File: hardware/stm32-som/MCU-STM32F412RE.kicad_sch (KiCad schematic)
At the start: 33 parts

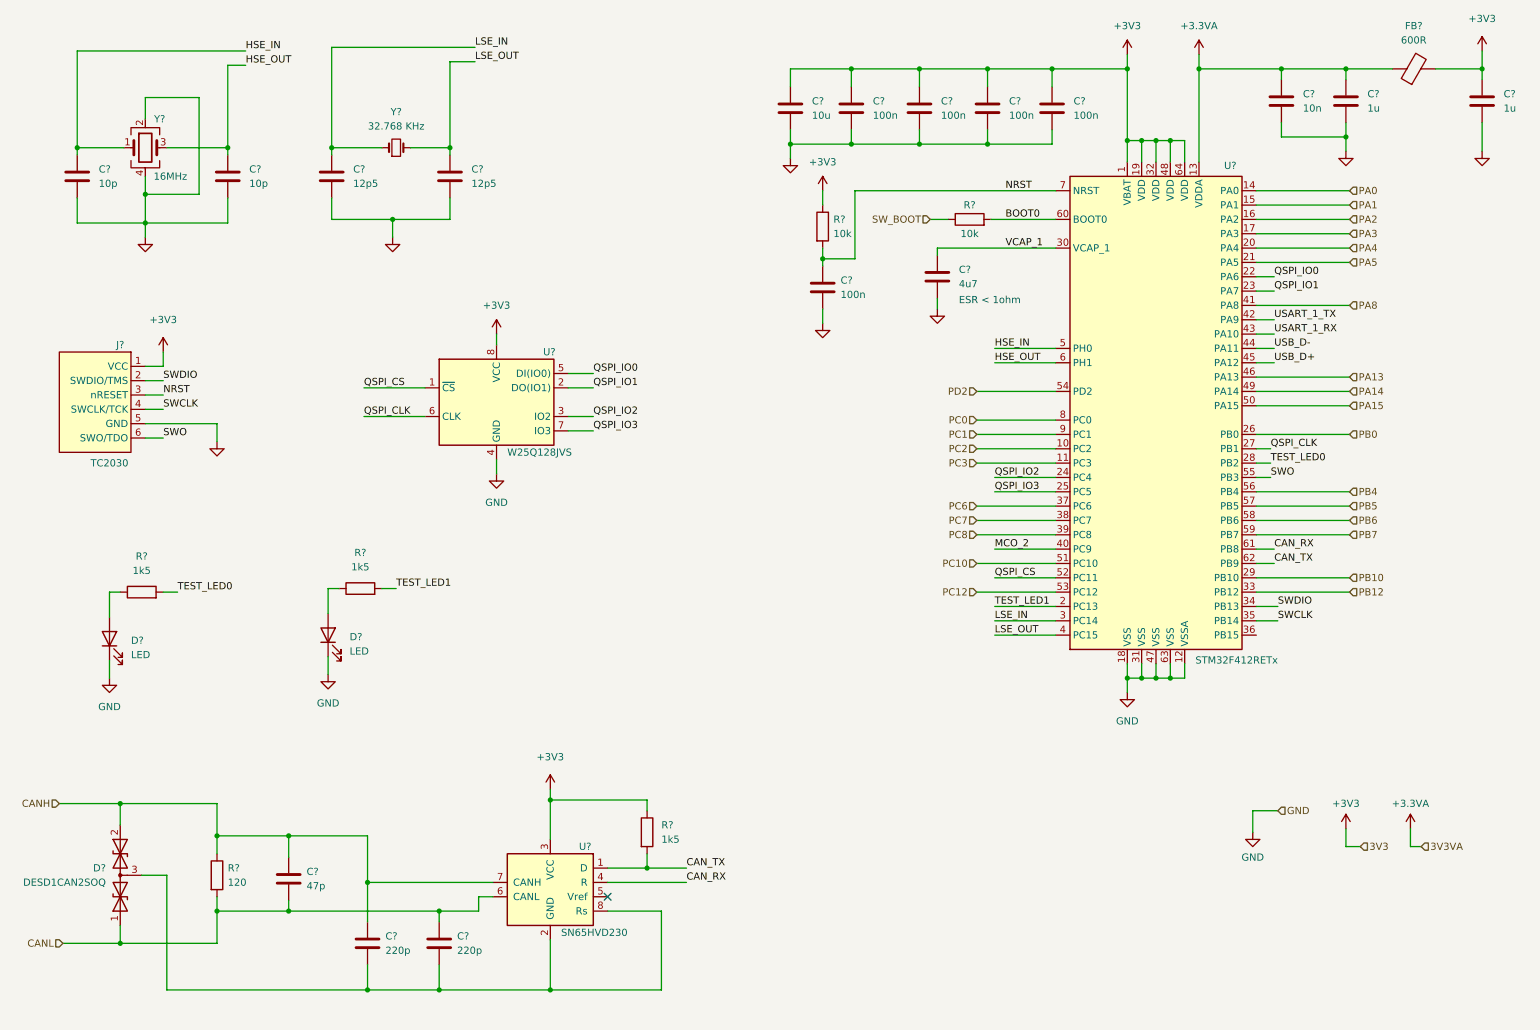
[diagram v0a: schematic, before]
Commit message: add test points, complete top hierarchical level, correct jtag mcu connection
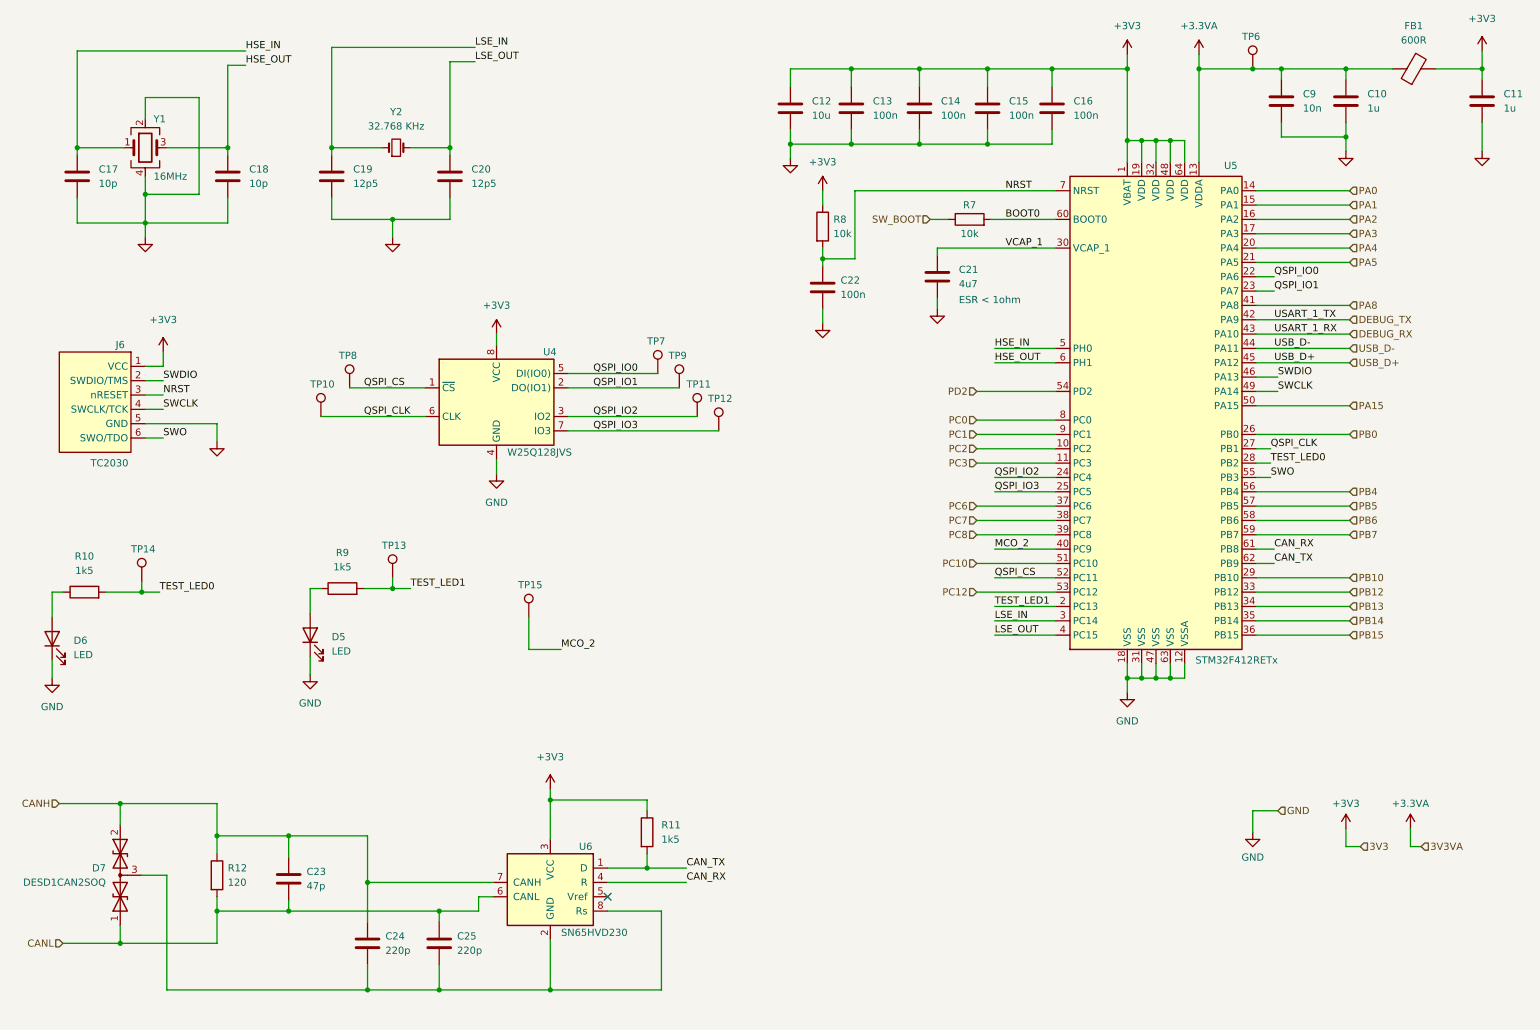
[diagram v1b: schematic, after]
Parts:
- added TP10, TP11, TP12, TP13, TP14, TP15, TP6, TP7, TP8, TP9: TestPoint, symbol Connector:TestPoint
- gave numbers to parts that had none: 33
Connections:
- net PA13 is gone; now on net SWDIO: U5.46 (PA13)
- net PA14 is gone; now on net SWCLK: U5.49 (PA14)
- net +3.3VA: now also TP6.1
- net MCO_2: now also TP15.1
- net QSPI_CLK: now also TP10.1
- net QSPI_CS: now also TP8.1
- net QSPI_IO0: now also TP7.1
- net QSPI_IO1: now also TP9.1
- net QSPI_IO2: now also TP11.1
- net QSPI_IO3: now also TP12.1
- net SWCLK: no longer U5.35 (PB14)
- net SWDIO: no longer U5.34 (PB13)
- net TEST_LED0: now also TP14.1
- net TEST_LED1: now also TP13.1
- net PB15: now reaches U5.36 (PB15)
- net USART_1_RX renamed DEBUG_RX
- net USART_1_TX renamed DEBUG_TX
- new net PB13: U5.34 (PB13)
- new net PB14: U5.35 (PB14)
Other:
- moved on the sheet: D5, D6, R10, R9

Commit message: clear ERC, small question about voltage level and rail timing on VCAP, but otherwise net name stuff
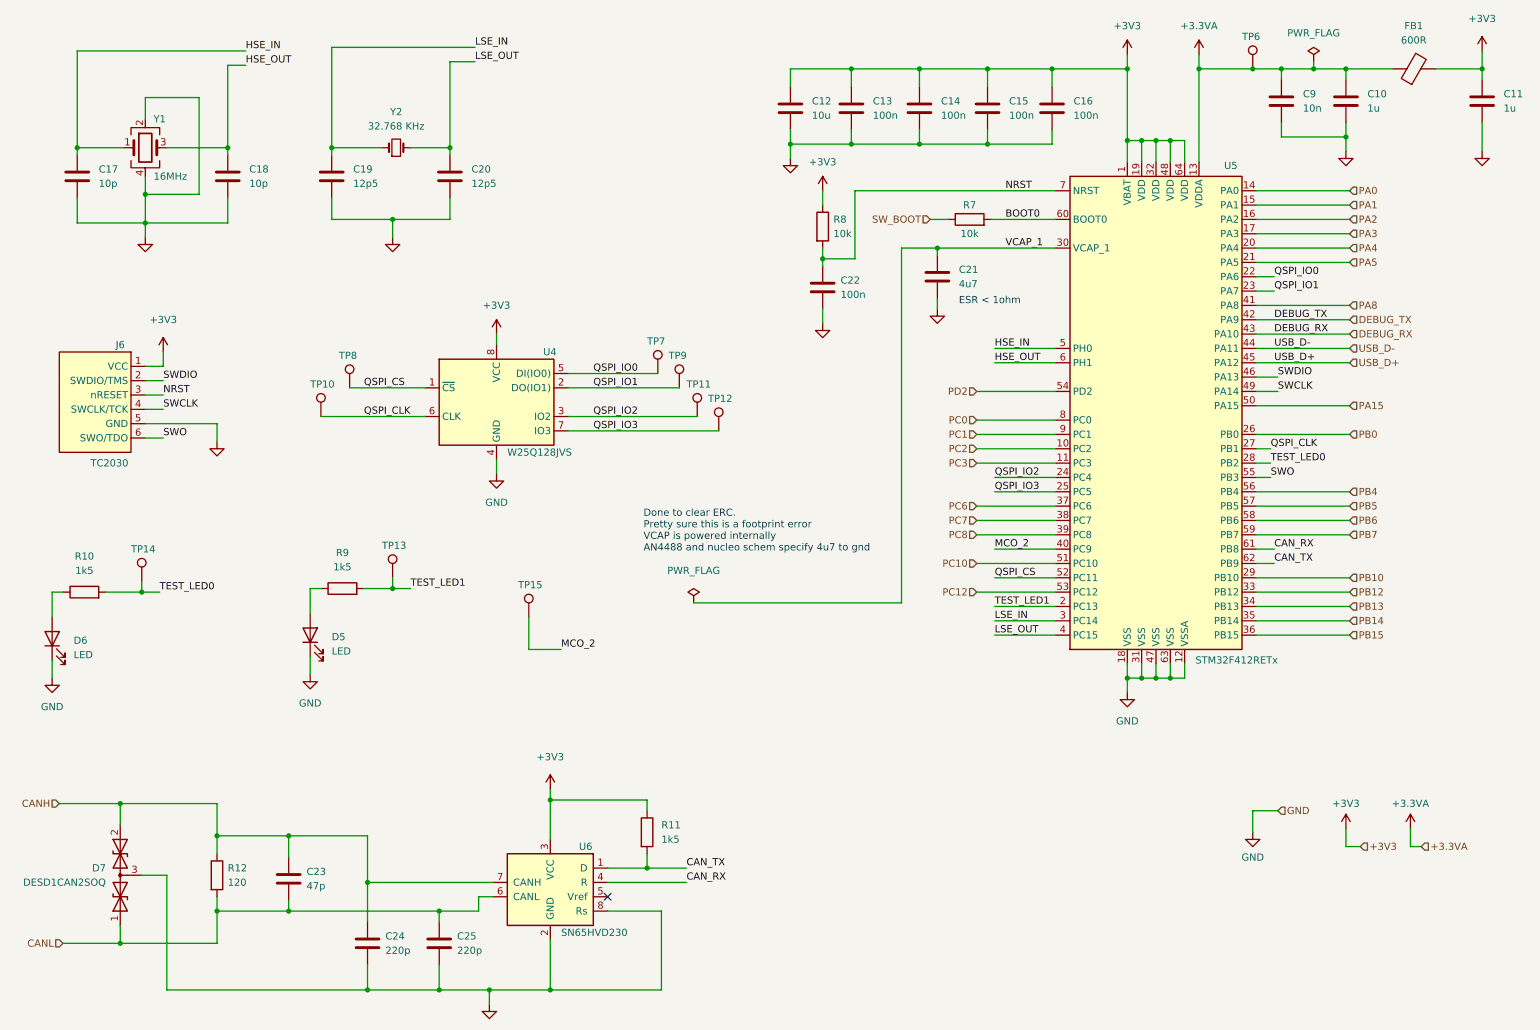
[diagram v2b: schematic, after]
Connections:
- net GND: now also C24.2, C25.2, D7.3 (common), U6.2 (GND), U6.8 (Rs)
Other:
- note added: "Done to clear ERC. Pretty sure this is a footprint error VCAP is powered internally AN4488 and nucleo schem specify 4u7 to gnd"
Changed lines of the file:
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@@
   (junction (at 79.375 168.275) (diameter 0) (color 0 0 0 0)
   )
+  (junction (at 180.34 55.88) (diameter 0) (color 0 0 0 0)
+  )
   (junction (at 83.82 50.8) (diameter 0) (color 0 0 0 0)
   )
@@
   (junction (at 189.23 37.465) (diameter 0) (color 0 0 0 0)
   )
+  (junction (at 100.965 187.325) (diameter 0) (color 0 0 0 0)
+  )
   (junction (at 165.1 37.465) (diameter 0) (color 0 0 0 0)
   )
@@
   )
   (junction (at 52.705 160.02) (diameter 0) (color 0 0 0 0)
+  )
+  (junction (at 247.015 24.13) (diameter 0) (color 0 0 0 0)
   )
   (junction (at 241.3 24.13) (diameter 0) (color 0 0 0 0)
@@
     (stroke (width 0) (type default) (color 0 0 0 0))
   )
+  (wire (pts (xy 173.99 55.88) (xy 180.34 55.88))
+    (stroke (width 0) (type default) (color 0 0 0 0))
+  )
   (wire (pts (xy 177.165 34.925) (xy 177.165 37.465))
     (stroke (width 0) (type default) (color 0 0 0 0))
@@
     (stroke (width 0) (type default) (color 0 0 0 0))
   )
+  (wire (pts (xy 247.015 24.13) (xy 252.73 24.13))
+    (stroke (width 0) (type default) (color 0 0 0 0))
+  )
   (wire (pts (xy 111.76 153.67) (xy 128.905 153.67))
     (stroke (width 0) (type default) (color 0 0 0 0))
@@
     (stroke (width 0) (type default) (color 0 0 0 0))
   )
+  (wire (pts (xy 100.965 187.325) (xy 100.965 189.865))
+    (stroke (width 0) (type default) (color 0 0 0 0))
+  )
   (wire (pts (xy 107.95 121.285) (xy 107.95 127))
     (stroke (width 0) (type default) (color 0 0 0 0))
@@
     (stroke (width 0) (type default) (color 0 0 0 0))
   )
+  (wire (pts (xy 100.965 187.325) (xy 111.76 187.325))
+    (stroke (width 0) (type default) (color 0 0 0 0))
+  )
   (wire (pts (xy 200.66 34.925) (xy 200.66 37.465))
     (stroke (width 0) (type default) (color 0 0 0 0))
@@
     (stroke (width 0) (type default) (color 0 0 0 0))
   )
+  (wire (pts (xy 173.99 55.88) (xy 173.99 118.745))
+    (stroke (width 0) (type default) (color 0 0 0 0))
+  )
   (wire (pts (xy 213.995 129.54) (xy 213.995 132.08))
     (stroke (width 0) (type default) (color 0 0 0 0))
@@
     (stroke (width 0) (type default) (color 0 0 0 0))
   )
-  (wire (pts (xy 241.3 24.13) (xy 252.73 24.13))
+  (wire (pts (xy 241.3 24.13) (xy 247.015 24.13))
     (stroke (width 0) (type default) (color 0 0 0 0))
   )
@@
     (stroke (width 0) (type default) (color 0 0 0 0))
   )
-  (wire (pts (xy 92.075 187.325) (xy 111.76 187.325))
+  (wire (pts (xy 92.075 187.325) (xy 100.965 187.325))
     (stroke (width 0) (type default) (color 0 0 0 0))
   )
@@
     (stroke (width 0) (type default) (color 0 0 0 0))
   )
+  (wire (pts (xy 247.015 22.86) (xy 247.015 24.13))
+    (stroke (width 0) (type default) (color 0 0 0 0))
+  )
   (wire (pts (xy 35.56 158.115) (xy 35.56 154.305))
     (stroke (width 0) (type default) (color 0 0 0 0))
@@
     (stroke (width 0) (type default) (color 0 0 0 0))
   )
+  (wire (pts (xy 173.99 118.745) (xy 137.16 118.745))
+    (stroke (width 0) (type default) (color 0 0 0 0))
+  )
   (wire (pts (xy 213.995 36.83) (xy 216.535 36.83))
     (stroke (width 0) (type default) (color 0 0 0 0))
@@
     (stroke (width 0) (type default) (color 0 0 0 0))
   )
+  (text "Done to clear ERC.\nPretty sure this is a footprint error\nVCAP is powered internally\nAN4488 and nucleo schem specify 4u7 to gnd"
+    (at 128.27 109.855 0)
+    (effects (font (size 1.27 1.27)) (justify left bottom))
+  )
   (text "ESR < 1ohm" (at 184.15 66.04 0)
     (effects (font (size 1.27 1.27)) (justify left bottom))
@@
     (effects (font (size 1.27 1.27)) (justify left bottom))
   )
-  (label "USART_1_TX" (at 240.03 68.58 0)
+  (label "DEBUG_TX" (at 240.03 68.58 0)
     (effects (font (size 1.27 1.27)) (justify left bottom))
   )
@@
     (effects (font (size 1.27 1.27)) (justify left bottom))
   )
-  (label "USART_1_RX" (at 240.03 71.12 0)
+  (label "DEBUG_RX" (at 240.03 71.12 0)
     (effects (font (size 1.27 1.27)) (justify left bottom))
   )
@@
     (effects (font (size 1.27 1.27)) (justify left))
   )
-  (hierarchical_label "3V3" (shape input) (at 255.27 161.925 0)
+  (hierarchical_label "+3V3" (shape input) (at 255.27 161.925 0)
     (effects (font (size 1.27 1.27)) (justify left))
   )
@@
     (effects (font (size 1.27 1.27)) (justify left))
   )
-  (hierarchical_label "3V3VA" (shape input) (at 266.065 161.925 0)
+  (hierarchical_label "+3.3VA" (shape input) (at 266.065 161.925 0)
     (effects (font (size 1.27 1.27)) (justify left))
   )
@@
     )
     (property "Datasheet" "" (id 3) (at 52.705 90.17 0)
+      (effects (font (size 1.27 1.27)) hide)
+    )
+    (pin "1")
+  )
+  (symbol (lib_id "power:PWR_FLAG") (at 247.015 22.86 0) (unit 1)
+    (in_bom yes) (on_board yes) (fields_autoplaced)
+    (property "Reference" "#FLG0104" (id 0) (at 247.015 20.955 0)
+      (effects (font (size 1.27 1.27)) hide)
+    )
+    (property "Value" "PWR_FLAG" (id 1) (at 247.015 17.78 0))
+    (property "Footprint" "" (id 2) (at 247.015 22.86 0)
+      (effects (font (size 1.27 1.27)) hide)
+    )
+    (property "Datasheet" "~" (id 3) (at 247.015 22.86 0)
       (effects (font (size 1.27 1.27)) hide)
     )
@@
     (pin "2")
   )
+  (symbol (lib_id "power:GND") (at 100.965 189.865 0) (unit 1)
+    (in_bom yes) (on_board yes) (fields_autoplaced)
+    (property "Reference" "#PWR0101" (id 0) (at 100.965 196.215 0)
+      (effects (font (size 1.27 1.27)) hide)
+    )
+    (property "Value" "GND" (id 1) (at 100.965 194.31 0)
+      (effects (font (size 1.27 1.27)) hide)
+    )
+    (property "Footprint" "" (id 2) (at 100.965 189.865 0)
+      (effects (font (size 1.27 1.27)) hide)
+    )
+    (property "Datasheet" "" (id 3) (at 100.965 189.865 0)
+      (effects (font (size 1.27 1.27)) hide)
+    )
+    (pin "1")
+  )
+  (symbol (lib_id "power:PWR_FLAG") (at 137.16 118.745 0) (unit 1)
+    (in_bom yes) (on_board yes) (fields_autoplaced)
+    (property "Reference" "#FLG0106" (id 0) (at 137.16 116.84 0)
+      (effects (font (size 1.27 1.27)) hide)
+    )
+    (property "Value" "PWR_FLAG" (id 1) (at 137.16 113.03 0))
+    (property "Footprint" "" (id 2) (at 137.16 118.745 0)
+      (effects (font (size 1.27 1.27)) hide)
+    )
+    (property "Datasheet" "~" (id 3) (at 137.16 118.745 0)
+      (effects (font (size 1.27 1.27)) hide)
+    )
+    (pin "1")
+  )
   (symbol (lib_id "power:+3V3") (at 102.235 71.12 0) (unit 1)

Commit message: add footprints to all components, JLC part numbers to to everything except capacitors and resistors
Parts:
- C10, C11, C21: footprint (none) -> Capacitor_SMD:C_0603_1608Metric
- C12: footprint (none) -> Capacitor_SMD:C_0805_2012Metric
- C13, C14, C15, C16, C17, C18, C19, C20, C22, C23, C24, C25, C9: footprint (none) -> Capacitor_SMD:C_0402_1005Metric
- D5, D6: footprint (none) -> LED_SMD:LED_0603_1608Metric; JLC (none) -> C2286
- D7: footprint (none) -> Package_TO_SOT_SMD:SOT-23; JLC (none) -> C508188
- FB1: footprint (none) -> Inductor_SMD:L_0603_1608Metric; JLC (none) -> C1002
- R10, R11, R7, R8, R9: footprint (none) -> Resistor_SMD:R_0402_1005Metric
- R12: footprint (none) -> Resistor_SMD:R_1206_3216Metric
- TP10, TP11, TP12, TP13, TP14, TP15, TP6, TP7, TP8, TP9: footprint (none) -> TestPoint:TestPoint_Loop_D2.54mm_Drill1.5mm_Beaded
- Y1: footprint (none) -> Crystal:Crystal_SMD_3225-4Pin_3.2x2.5mm; JLC (none) -> C112972
- Y2: footprint (none) -> Crystal:Crystal_SMD_3215-2Pin_3.2x1.5mm

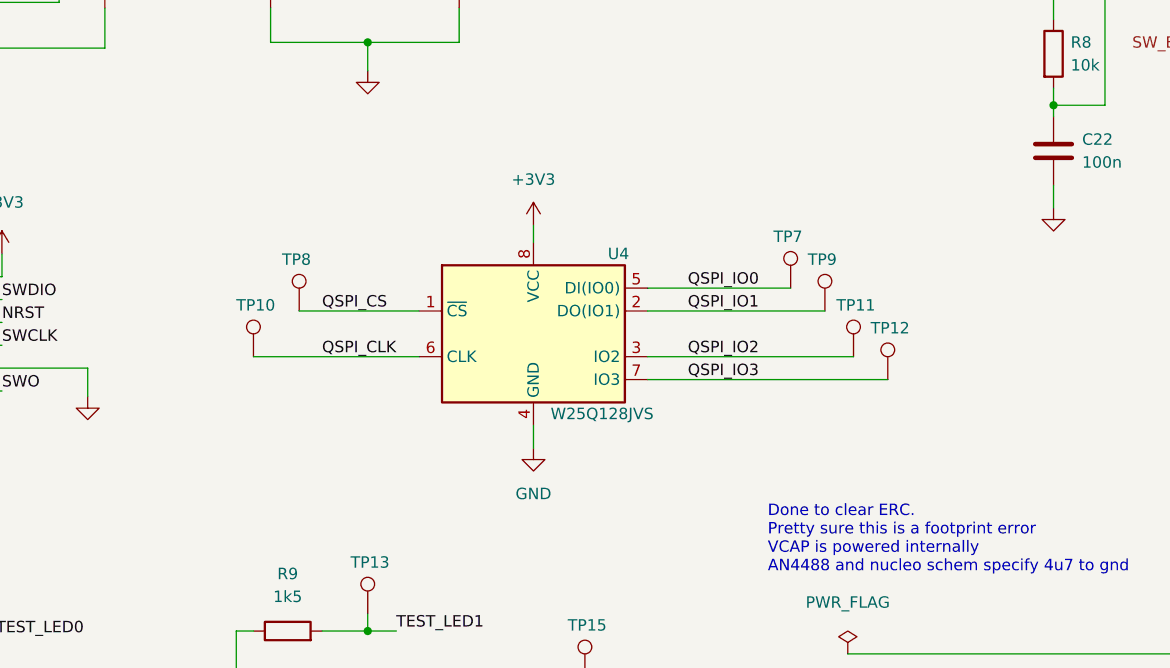
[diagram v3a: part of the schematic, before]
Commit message: swap big qspi test points for small test header, complete rough layout
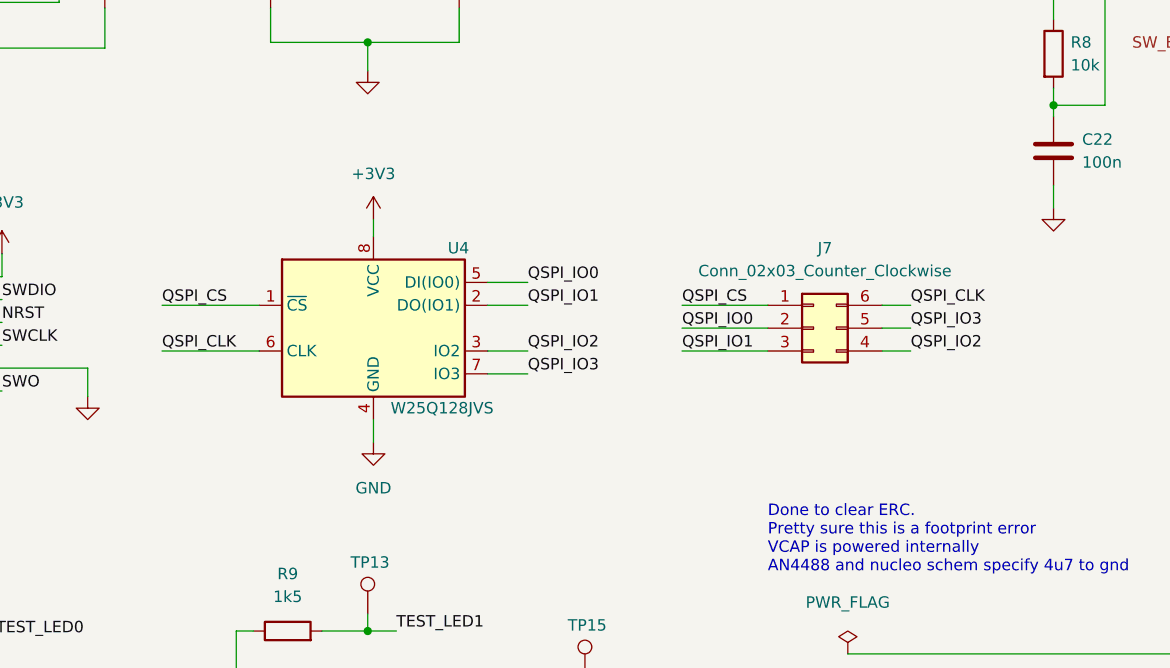
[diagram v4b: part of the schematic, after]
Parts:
- removed TP10, TP11, TP12, TP7, TP8, TP9: TestPoint, TestPoint:TestPoint_Loop_D2.54mm_Drill1.5mm_Beaded, symbol Connector:TestPoint
- added J7: Conn_02x03_Counter_Clockwise, Connector_PinHeader_1.27mm:PinHeader_2x03_P1.27mm_Vertical_SMD, symbol Connector_Generic:Conn_02x03_Counter_Clockwise
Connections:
- net QSPI_CLK: now also J7.6 (Pin_6)
- net QSPI_CS: now also J7.1 (Pin_1)
- net QSPI_IO0: now also J7.2 (Pin_2)
- net QSPI_IO1: now also J7.3 (Pin_3)
- net QSPI_IO2: now also J7.4 (Pin_4)
- net QSPI_IO3: now also J7.5 (Pin_5)
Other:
- moved on the sheet: U4
